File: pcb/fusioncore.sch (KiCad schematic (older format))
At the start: 68 parts, among them J1 Conn_02x12_Top_Bottom, J10 Pump_Misc_1, J11 Pump_Misc_2, J12 Flow_Warm, J13 Flow_Cold, J14 Trigger, J15 Valve_M1, J16 Valve_M2, J17 Valve_M3, J18 Valve_M4, J19 Valve_Air_Lime, J2 Temp_1, J20 Valve_Air_Rum, J21 Valve_Air_Out, J22 LED, J3 40HAT, J4 Temp_2, J6 Pump_Water_Cold, J7 Pump_Water_Warm, J8 Pump_Air, J9 CONN_01X02, Q1 DMG2305UX, Q10 AO3400A, Q11 AO3400A, Q12 AO3400A, Q13 AO3400A, Q14 AO3400A, Q2 DMMT5401, Q3 AO3400A, Q4 AO3400A, Q5 AO3400A, Q6 AO3400A, Q7 AO3400A, Q8 AO3400A, Q9 AO3400A, SW1 POWER_ON, U1 74HC244, U2 CAT24C32

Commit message: Working on PCB schematic
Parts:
- removed U1: 74HC244, project_footprints:SOIC127P1032X265-20N, symbol 74xx:74HC244
- added C1, C3, C4: 0.1μF, symbol Device:C
- added C2, C5: 10μF, symbol Device:C
- added J5: WEIGHT, symbol Connector_Generic:Conn_01x04
- added Q15: BSS138, Package_TO_SOT_SMD:SOT-23, symbol Transistor_FET:BSS138
- added Q16: S8550, Package_TO_SOT_THT:TO-92_Inline, symbol Transistor_BJT:S8550
- added Q17, Q18: AO3400A, Package_TO_SOT_SMD:SOT-23, symbol Transistor_FET:2N7002
- added R10, R9: 10K, symbol Device:R
- added R12, R13: 100, symbol Device:R
- added R14: 20K, symbol Device:R
- added R15: 8.2K, symbol Device:R
- added R16, R17, R18, R19, R20, R21, R22, R25, R26, R27: R, symbol Device:R
- added U1: HX711, Package_SO:SOP-16_4.55x10.3mm_P1.27mm, symbol misc:HX711
- added U3, U4: LTC2990, Package_SO:MSOP-10_3x3mm_P0.5mm, symbol Sensor:LTC2990
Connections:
- net labels added: 12V_ATX, 5V_ATX, I2C_SCL, I2C_SDA, Weight_CLK, Weight_D
- wire segments 306 -> 435
- no-connect marks 25 -> 11
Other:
- note added: "Current/Voltage Sensor"
- note added: "Weight"
- moved on the sheet: D10, D11, D12, D8, D9, J10, J11, J12, J13, J14, J2, J22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

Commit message: Working on the layout of pcb
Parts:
- added C6, C7: 0.1μF, Capacitor_SMD:C_0805_2012Metric_Pad1.15x1.40mm_HandSolder, symbol Device:C
- added R28, R32: 100K, Resistor_SMD:R_0805_2012Metric_Pad1.15x1.40mm_HandSolder, symbol Device:R
- added R30: 20K, Resistor_SMD:R_0805_2012Metric_Pad1.15x1.40mm_HandSolder, symbol Device:R
- added R31: 47K, Resistor_SMD:R_0805_2012Metric_Pad1.15x1.40mm_HandSolder, symbol Device:R
- added R33: DNP, Resistor_SMD:R_0805_2012Metric_Pad1.15x1.40mm_HandSolder, symbol Device:R
- added TP1: GND, TestPoint:TestPoint_Plated_Hole_D2.0mm, symbol Connector:TestPoint
- added TP2: 3V3_PI, TestPoint:TestPoint_Plated_Hole_D2.0mm, symbol Connector:TestPoint
- added TP3: 3V3, TestPoint:TestPoint_Plated_Hole_D2.0mm, symbol Connector:TestPoint
- added TP4: 5V, TestPoint:TestPoint_Plated_Hole_D2.0mm, symbol Connector:TestPoint
- added TP5: 12V, TestPoint:TestPoint_Plated_Hole_D2.0mm, symbol Connector:TestPoint
- C1, C2, C3, C4, C5: footprint (none) -> Capacitor_SMD:C_0805_2012Metric_Pad1.15x1.40mm_HandSolder
- D13: footprint (none) -> LED_SMD:LED_0603_1608Metric_Pad1.05x0.95mm_HandSolder
- D14: footprint (none) -> LED_SMD:LED_0805_2012Metric_Pad1.15x1.40mm_HandSolder
- J10, J11, J14, J15, J16, J17, J18, J19, J20, J21, J6, J7, J8: symbol Connector_Generic:Conn_01x02 -> Connector:Screw_Terminal_01x02
- J12, J13, J2, J22, J4: symbol Connector_Generic:Conn_01x03 -> Connector:Screw_Terminal_01x03
- J5: footprint (none) -> TerminalBlock_Phoenix:TerminalBlock_Phoenix_PT-1,5-4-5.0-H_1x04_P5.00mm_Horizontal; symbol Connector_Generic:Conn_01x04 -> Connector:Screw_Terminal_01x04
- R1: footprint Resistor_SMD:R_01005_0402Metric -> Resistor_SMD:R_0805_2012Metric_Pad1.15x1.40mm_HandSolder
- R10, R12, R13, R14, R15, R5, R7, R9: footprint (none) -> Resistor_SMD:R_0805_2012Metric_Pad1.15x1.40mm_HandSolder
- R11, R23, R24, R29, R6, R8: footprint Resistor_SMD:R_0603_1608Metric_Pad0.84x1.00mm_HandSolder -> Resistor_SMD:R_0805_2012Metric_Pad1.15x1.40mm_HandSolder
- R16: value R -> 0.15; footprint (none) -> Resistor_SMD:R_2512_6332Metric_Pad1.52x3.35mm_HandSolder
- R17, R18, R22, R26: value R -> 100K; footprint (none) -> Resistor_SMD:R_0805_2012Metric_Pad1.15x1.40mm_HandSolder
- R19, R20: value R -> 47K; footprint (none) -> Resistor_SMD:R_0805_2012Metric_Pad1.15x1.40mm_HandSolder
- R2, R3, R4: footprint Resistor_SMD:R_0603_1608Metric_Pad1.05x0.95mm_HandSolder -> Resistor_SMD:R_0805_2012Metric_Pad1.15x1.40mm_HandSolder
- R21, R27: value R -> 20K; footprint (none) -> Resistor_SMD:R_0805_2012Metric_Pad1.15x1.40mm_HandSolder
- R25: value R -> 0.03; footprint (none) -> Resistor_SMD:R_2512_6332Metric_Pad1.52x3.35mm_HandSolder
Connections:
- net 12V: now also R28.1, TP5.1; no longer U4.1 (V1)
- net 3V3: now also C6.2, C7.2, TP3.1
- net 3V3_PI: now also U4.1 (V1), TP2.1; no longer U4.3 (V3)
- net 5V: now also R32.2, R33.2, TP4.1; no longer U4.2 (V2)
- net 5V_PI: now also R33.1
- net GND: now also C6.1, C7.1, R30.2, R31.1, TP1.1
- net Pump_WC: now also J3.19 (BCM10); no longer J3.29 (BCM5)
- net Pump_WW: now also J3.21 (BCM9); no longer J3.31 (BCM6)
- net Weight_CLK: now also J3.29 (BCM5)
- net Weight_D: now also J3.31 (BCM6)
- net INA-: now reaches C4.1, R12.1, U1.7 (INA-)
- net INA+: now reaches C4.2, R13.1, U1.8 (INA+)
- net INA_C-: now reaches J5.2 (Pin_2), R12.2
- net INA_C+: now reaches J5.1 (Pin_1), R13.2
- new net: R31.2, R32.1, U4.2 (V2)
- new net: R28.2, R30.1, U4.3 (V3)
- no-connect marks 11 -> 9
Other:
- note added: "Testpoints"
- moved on the sheet: Q1, Q2A, Q2B, R23, R24, U4

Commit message: Almost done with PCB
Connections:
- net Flow_C: now also J3.18 (BCM24); no longer J3.16 (BCM23)
- net Flow_W: now also J3.16 (BCM23); no longer J3.18 (BCM24)
- net Pump_A: now also J3.40 (BCM21); no longer J3.33 (BCM13)
- net Pump_M2: now also J3.33 (BCM13); no longer J3.37 (BCM26)
- net Pump_WC: now also J3.37 (BCM26); no longer J3.19 (BCM10)
- net Pump_WW: now also J3.38 (BCM20); no longer J3.21 (BCM9)
- net Valve_AL: now also J3.19 (BCM10); no longer J3.36 (BCM16)
- net Valve_AO: now also J3.21 (BCM9); no longer J3.40 (BCM21)
- net Valve_AR: now also J3.23 (BCM11); no longer J3.38 (BCM20)
- net Valve_M1: now also J3.15 (BCM22); no longer J3.32 (BCM12)
- net Valve_M2: now also J3.13 (BCM27); no longer J3.11 (BCM17)
- net Valve_M3: now also J3.11 (BCM17); no longer J3.13 (BCM27)
- net Valve_M4: now also J3.10 (BCM15); no longer J3.15 (BCM22)
- no-connect marks 9 -> 8
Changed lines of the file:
@@
 	1900 2850 700  2850
 Wire Wire Line
-	1900 2950 700  2950
-Wire Wire Line
 	1900 3050 700  3050
-Text Label 700  2150 0    50   ~ 0
+Text Label 700  3050 0    50   ~ 0
 Pump_WC
-Text Label 700  2250 0    50   ~ 0
+Text Label 4300 3050 2    50   ~ 0
 Pump_WW
-Text Label 700  2850 0    50   ~ 0
+Text Label 4300 3150 2    50   ~ 0
 Pump_A
-Text Label 700  2950 0    50   ~ 0
-Pump_M1
-Text Label 700  3050 0    50   ~ 0
-Pump_M2
 Wire Wire Line
 	3100 2250 4300 2250
@@
 Wire Wire Line
 	3100 2050 4300 2050
+Text Label 4300 2050 2    50   ~ 0
+Flow_C
 Text Label 4300 1950 2    50   ~ 0
-Flow_C
-Text Label 4300 2050 2    50   ~ 0
 Flow_W
 Wire Wire Line
@@
 	3100 3050 4300 3050
 Wire Wire Line
-	3100 2950 4300 2950
-Text Label 4300 2950 2    50   ~ 0
+	700  2350 1900 2350
+Text Label 700  2150 0    50   ~ 0
 Valve_AL
-Text Label 4300 3050 2    50   ~ 0
+Text Label 700  2350 0    50   ~ 0
 Valve_AR
-Text Label 4300 3150 2    50   ~ 0
+Text Label 700  2250 0    50   ~ 0
 Valve_AO
 Wire Wire Line
-	3100 2750 4300 2750
-Text Label 4300 2750 2    50   ~ 0
+	3100 1650 4300 1650
+Text Label 700  1950 0    50   ~ 0
 Valve_M1
 Wire Wire Line
@@
 Wire Wire Line
 	1900 1950 700  1950
+Text Label 700  1850 0    50   ~ 0
+Valve_M2
 Text Label 700  1750 0    50   ~ 0
-Valve_M2
-Text Label 700  1850 0    50   ~ 0
 Valve_M3
-Text Label 700  1950 0    50   ~ 0
+Text Label 4300 1650 2    50   ~ 0
 Valve_M4
 Wire Wire Line
@@
 	1    0    0    -1
 $EndComp
-NoConn ~ 1900 2350
 NoConn ~ 3100 2450
 NoConn ~ 3100 2350
-NoConn ~ 3100 1650
 NoConn ~ 3100 1550
 Wire Wire Line
@@
 Text Label 4100 10750 0    50   ~ 0
 INAR+
+Text Label 700  2850 0    50   ~ 0
+Pump_M2
+Text Label 700  2950 0    50   ~ 0
+Pump_M1
+Wire Wire Line
+	1900 2950 700  2950
+NoConn ~ 3100 2750
 $EndSCHEMATC

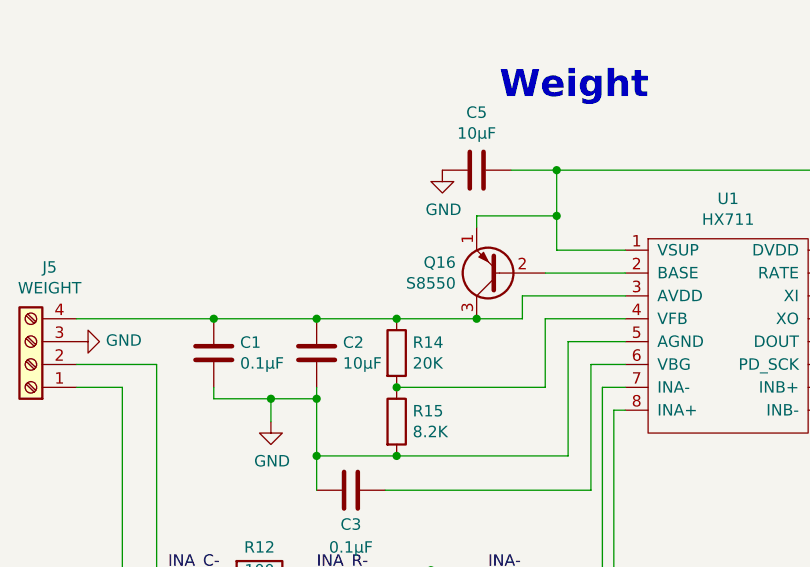
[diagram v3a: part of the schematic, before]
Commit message: Changed Hx711 transistor
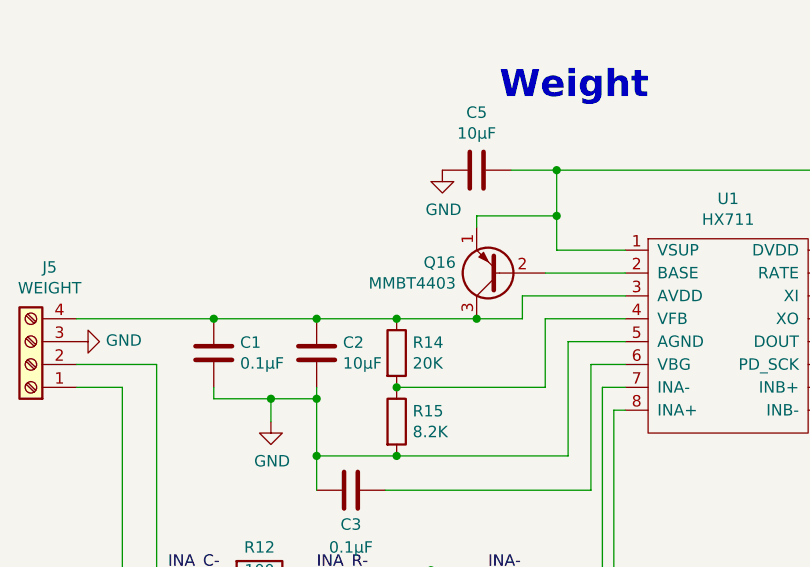
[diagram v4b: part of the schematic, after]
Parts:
- Q16: value S8550 -> MMBT4403; footprint Package_TO_SOT_THT:TO-92_Inline -> Package_TO_SOT_SMD:SOT-23
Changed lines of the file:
@@
 P 4900 9150
 F 0 "Q16" H 5091 9104 50  0000 L CNN
-F 1 "S8550" H 5091 9195 50  0000 L CNN
-F 2 "Package_TO_SOT_THT:TO-92_Inline" H 5100 9075 50  0001 L CIN
-F 3 "http://www.unisonic.com.tw/datasheet/S8550.pdf" H 4900 9150 50  0001 L CNN
+F 1 "MMBT4403" H 5091 9195 50  0000 L CNN
+F 2 "Package_TO_SOT_SMD:SOT-23" H 5100 9075 50  0001 L CIN
+F 3 "https://datasheet.lcsc.com/szlcsc/Guangdong-Hottech-MMBT4403_C181124.pdf" H 4900 9150 50  0001 L CNN
 	1    4900 9150
 	-1   0    0    1

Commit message: Fixed component sizes and rearranged components to match spec
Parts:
- Q1: LCSC (none) -> C144153
- Q16: LCSC (none) -> C8513
- Q2: LCSC (none) -> C154733
- R5, R7: LCSC (none) -> C17471
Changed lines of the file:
@@
 F 2 "Package_TO_SOT_SMD:SOT-23" H 6400 2000 50  0001 C CNN
 F 3 "" H 6200 1900 50  0000 C CNN
+F 4 "C144153" V 6200 1900 50  0001 C CNN "LCSC"
 	1    6200 1900
 	0    -1   -1   0
@@
 F 2 "Package_TO_SOT_SMD:SOT-23-6" H 6100 2425 50  0000 L CIN
 F 3 "" H 5900 2500 50  0000 L CNN
+F 4 "C154733" H 5900 2500 50  0001 C CNN "LCSC"
 	1    5900 2500
 	-1   0    0    1
@@
 F 2 "Package_TO_SOT_SMD:SOT-23-6" H 6700 2425 50  0000 L CIN
 F 3 "" H 6500 2500 50  0000 L CNN
+F 4 "C154733" H 6500 2500 50  0001 C CNN "LCSC"
 	2    6500 2500
 	1    0    0    1
@@
 F 2 "Resistor_SMD:R_0805_2012Metric_Pad1.15x1.40mm_HandSolder" V 11480 2100 50  0001 C CNN
 F 3 "~" H 11550 2100 50  0001 C CNN
+F 4 "C17471" V 11550 2100 50  0001 C CNN "LCSC"
 	1    11550 2100
 	0    1    1    0
@@
 F 2 "Resistor_SMD:R_0805_2012Metric_Pad1.15x1.40mm_HandSolder" V 11480 2300 50  0001 C CNN
 F 3 "~" H 11550 2300 50  0001 C CNN
+F 4 "C17471" V 11550 2300 50  0001 C CNN "LCSC"
 	1    11550 2300
 	0    1    1    0
@@
 F 2 "Package_TO_SOT_SMD:SOT-23" H 5100 9075 50  0001 L CIN
 F 3 "https://datasheet.lcsc.com/szlcsc/Guangdong-Hottech-MMBT4403_C181124.pdf" H 4900 9150 50  0001 L CNN
+F 4 "C8513" H 4900 9150 50  0001 C CNN "LCSC"
 	1    4900 9150
 	-1   0    0    1

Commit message: Added LSCS part numbers
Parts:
- C1, C3, C4, C6, C7: LCSC (none) -> C49678
- C2, C5: LCSC (none) -> C15850
- D1, D10, D11, D12, D2, D3, D4, D5, D6, D7, D8, D9: LCSC (none) -> C64898
- D13: LCSC (none) -> C72043
- D14: LCSC (none) -> C2296
- Q10, Q11, Q12, Q13, Q14, Q17, Q18, Q3, Q4, Q5, Q6, Q7, Q8, Q9: symbol Transistor_FET:2N7002 -> misc:AO3400A; LCSC (none) -> C20917
- R1: LCSC (none) -> C17673
- R10, R2, R23, R29, R3, R4, R9: LCSC (none) -> C17414
- R14, R21, R27, R30: LCSC (none) -> C4328
- R15: LCSC (none) -> C17828
- R16: LCSC (none) -> C247454
- R17, R18, R22, R26, R28, R32: LCSC (none) -> C17407
- R19, R20, R24, R31: LCSC (none) -> C17713
- R25: LCSC (none) -> C87220
- R6, R8: LCSC (none) -> C17614
- U1: LCSC (none) -> C43656
- U3, U4: LCSC (none) -> C107804

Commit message: Minor PCB fixes.
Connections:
- no-connect marks 8 -> 9
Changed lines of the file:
@@
 	1900 2950 700  2950
 NoConn ~ 3100 2750
+NoConn ~ 3100 2950
 $EndSCHEMATC

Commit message: Added logic level shifter to schema only.
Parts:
- removed Q15: BSS138, Package_TO_SOT_SMD:SOT-23, symbol Transistor_FET:BSS138
- removed Q17, Q18: AO3400A, Package_TO_SOT_SMD:SOT-23, symbol misc:AO3400A
- removed R10, R9: 10K, Resistor_SMD:R_0805_2012Metric_Pad1.15x1.40mm_HandSolder, symbol Device:R
- added U?: TXB0108DQSR, Package_SON:USON-20_2x4mm_P0.4mm, symbol Logic_LevelTranslator:TXB0108DQSR
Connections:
- net 12V: no longer J12.1 (Pin_1), J13.1 (Pin_1)
- net 3V3: now also U?.5 (VCCA)
- net 5V: now also J12.1 (Pin_1), J13.1 (Pin_1), U?.16 (VCCB)
- net Flow_C: now also U?.3 (A3)
- net Flow_W: now also U?.2 (A2)
- net GND: now also U?.15 (GND)
- net LED_PWM: now also U?.1 (A1)
- net Flow_C_5V: now reaches J13.2 (Pin_2), R3.2
- net Flow_C_5V: now also U?.18 (B3)
- net Flow_W_5V: now reaches J12.2 (Pin_2), R2.1
- net Flow_W_5V: now also U?.19 (B2)
- net LED_PWM_5V: now reaches J22.2 (Pin_2)
- net LED_PWM_5V: now also U?.20 (B1)
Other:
- note added: "3V3 5V Shifter"
- note removed: "Pullup Resistors"
- note removed: "These are just pullup resistors for the I2C bus on the EEPROM.\nThe resistor values are per the HAT spec."
- moved on the sheet: C7, D13, D14, J1, J22, R5, R6, R7, R8, SW1
